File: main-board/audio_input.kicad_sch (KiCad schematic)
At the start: 46 parts, among them J4 NCJ6FA-H-0, J6 NCJ6FA-H-0, Q1 MMBT3904, Q2 MMBT3906, Q3 MMBT3906, Q4 MMBT3904, U4 THAT1246, U5 THAT1246, U6 OPA1656ID, U7 LM2903

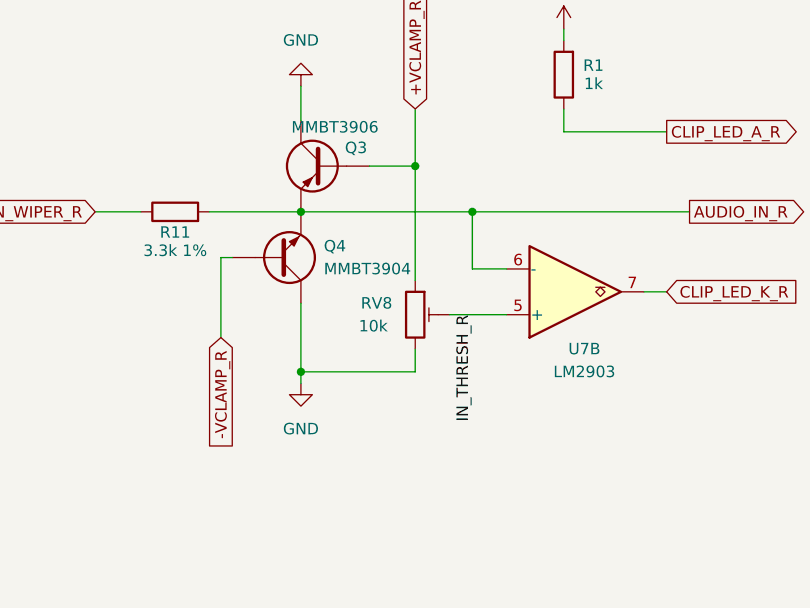
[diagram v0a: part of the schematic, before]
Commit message: swap and label rv8/7 so they lay out clearly
fixes #21
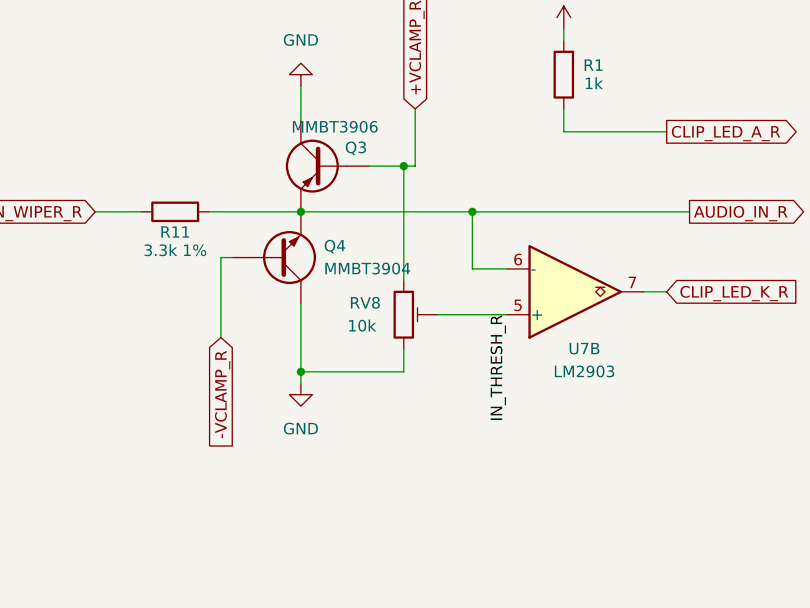
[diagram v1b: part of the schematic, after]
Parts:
- RV7: Label (none) -> ICT_L
- RV8: Label (none) -> ICT_R
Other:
- moved on the sheet: RV8
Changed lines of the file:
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@@
 	)
 	(junction
+		(at 170.18 104.14)
+		(diameter 0)
+		(color 0 0 0 0)
+	)
+	(junction
 		(at 88.9 166.37)
 		(diameter 0)
@@
 	)
 	(junction
-		(at 171.45 104.14)
-		(diameter 0)
-		(color 0 0 0 0)
-	)
-	(junction
 		(at 48.26 149.86)
 		(diameter 0)
@@
 	(wire
 		(pts
-			(xy 166.37 104.14) (xy 171.45 104.14)
+			(xy 166.37 104.14) (xy 170.18 104.14)
 		)
 		(stroke
@@
 	(wire
 		(pts
-			(xy 175.26 120.65) (xy 181.61 120.65)
+			(xy 173.99 120.65) (xy 181.61 120.65)
 		)
 		(stroke
@@
 	(wire
 		(pts
-			(xy 171.45 116.84) (xy 171.45 104.14)
+			(xy 170.18 116.84) (xy 170.18 104.14)
 		)
 		(stroke
@@
 	(wire
 		(pts
-			(xy 171.45 124.46) (xy 171.45 127)
+			(xy 170.18 124.46) (xy 170.18 127)
 		)
 		(stroke
@@
 	(wire
 		(pts
-			(xy 171.45 127) (xy 158.75 127)
+			(xy 170.18 127) (xy 158.75 127)
 		)
 		(stroke
@@
 	(wire
 		(pts
+			(xy 170.18 104.14) (xy 171.45 104.14)
+		)
+		(stroke
+			(width 0)
+			(type default)
+		)
+	)
+	(wire
+		(pts
 			(xy 135.89 166.37) (xy 135.89 172.72)
 		)
@@
 	)
 	(label "IN_THRESH_R"
-		(at 177.8 120.65 270)
+		(at 181.61 120.65 270)
 		(effects
 			(font
@@
 		(lib_name "R_Potentiometer_Trim_1")
 		(lib_id "Device:R_Potentiometer_Trim")
-		(at 171.45 120.65 0)
+		(at 170.18 120.65 0)
 		(unit 1)
 		(exclude_from_sim no)
@@
 		(dnp no)
 		(property "Reference" "RV8"
-			(at 168.91 119.3799 0)
+			(at 167.64 119.3799 0)
 			(effects
 				(font
@@
 		)
 		(property "Value" "10k"
-			(at 168.402 121.92 0)
+			(at 167.132 121.92 0)
 			(effects
 				(font
@@
 		)
 		(property "Footprint" "Potentiometer_THT:Potentiometer_Bourns_3296W_Vertical"
-			(at 171.45 120.65 0)
+			(at 170.18 120.65 0)
 			(effects
 				(font
@@
 		)
 		(property "Datasheet" "~"
-			(at 171.45 120.65 0)
+			(at 170.18 120.65 0)
 			(effects
 				(font
@@
 		)
 		(property "Description" "Multi-Turn Trim-potentiometer"
-			(at 171.45 120.65 0)
+			(at 170.18 120.65 0)
+			(effects
+				(font
+					(size 1.27 1.27)
+				)
+				(hide yes)
+			)
+		)
+		(property "Label" "ICT_R"
+			(at 170.942 124.46 0)
 			(effects
 				(font
@@
 			(at 171.45 58.42 0)
 			(effects
+				(font
+					(size 1.27 1.27)
+				)
+				(hide yes)
+			)
+		)
+		(property "Label" "ICT_L"
+			(at 171.45 58.42 0)
+			(effects

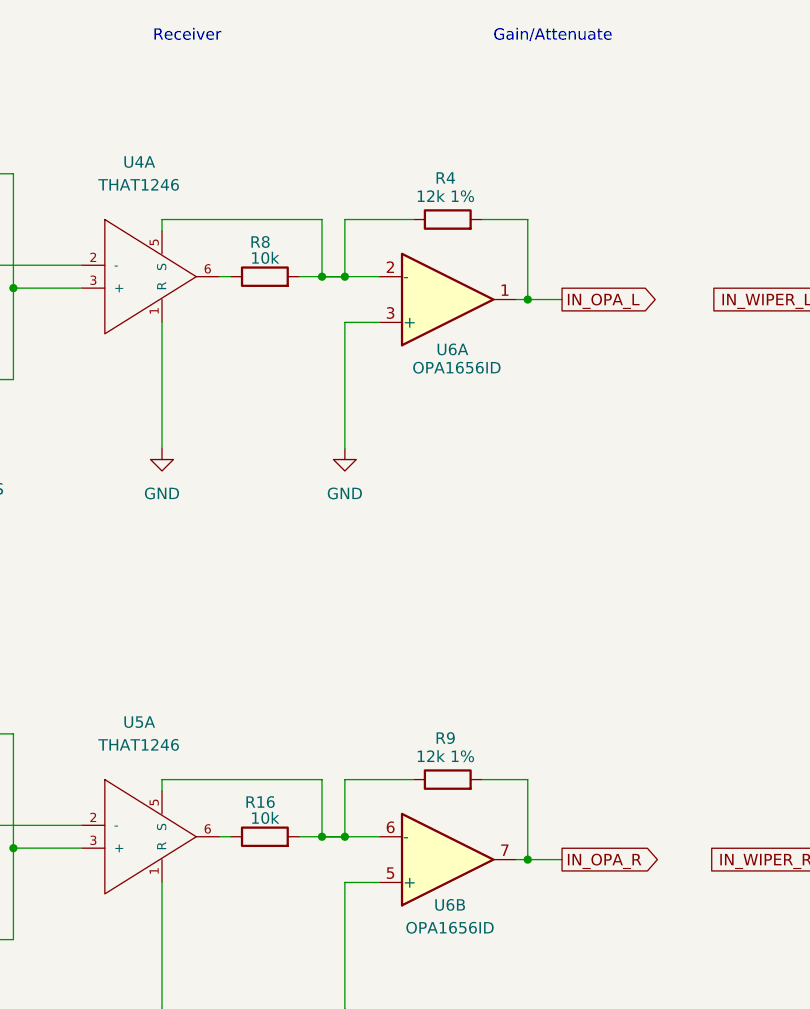
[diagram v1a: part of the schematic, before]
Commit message: fix sense error for output topology
fixes #20
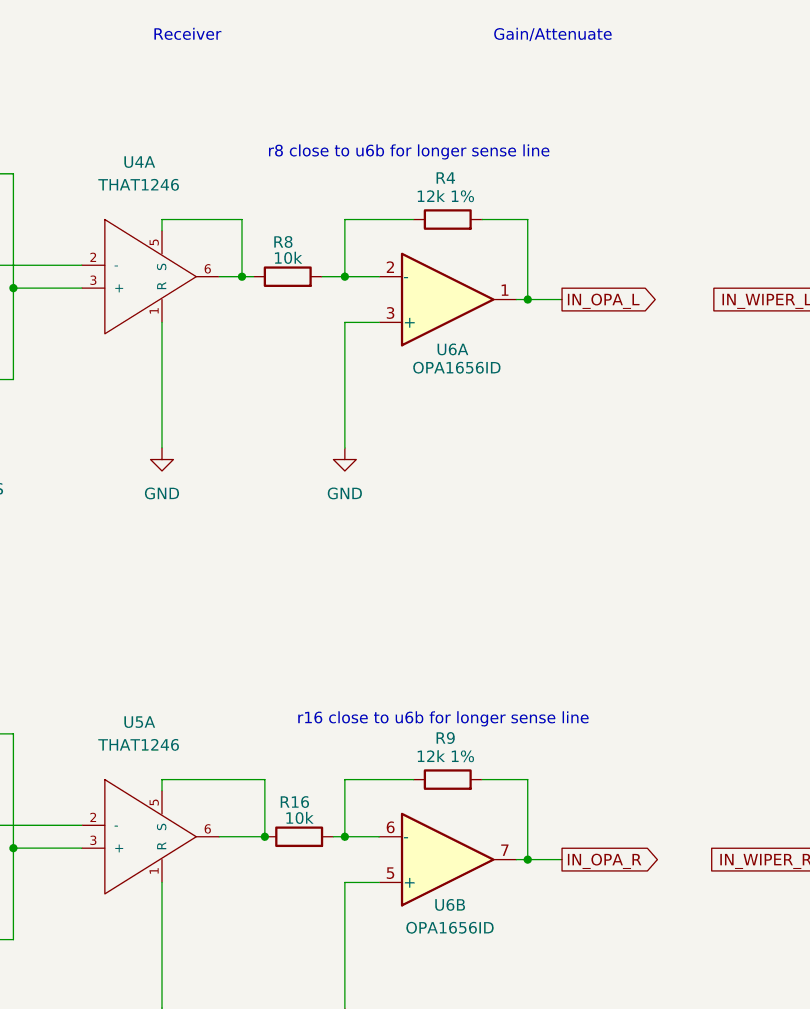
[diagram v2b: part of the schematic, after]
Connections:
- net at R16.2, R9.1, U6.6 (-): no longer U5.5 (S)
- net at R4.1, R8.2, U6.2 (-): no longer U4.5 (S)
- net at R8.1, U4.6: now also U4.5 (S)
- net at R16.1, U5.6: now also U5.5 (S)
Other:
- note added: "r16 close to u6b for longer sense line"
- note added: "r8 close to u6b for longer sense line"
- moved on the sheet: R16, R8
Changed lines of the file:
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@@
 		)
 	)
+	(text "r16 close to u6b for longer sense line\n"
+		(exclude_from_sim no)
+		(at 93.472 93.726 0)
+		(effects
+			(font
+				(size 1.27 1.27)
+			)
+		)
+	)
 	(text "Clipper Reference\n"
 		(exclude_from_sim no)
@@
 		)
 	)
+	(text "r8 close to u6b for longer sense line\n"
+		(exclude_from_sim no)
+		(at 89.662 30.734 0)
+		(effects
+			(font
+				(size 1.27 1.27)
+			)
+		)
+	)
 	(junction
 		(at 170.18 104.14)
@@
 	)
 	(junction
+		(at 73.66 106.68)
+		(diameter 0)
+		(color 0 0 0 0)
+	)
+	(junction
 		(at 88.9 173.99)
 		(diameter 0)
@@
 	)
 	(junction
-		(at 80.01 106.68)
+		(at 45.72 45.72)
 		(diameter 0)
 		(color 0 0 0 0)
 	)
 	(junction
-		(at 45.72 45.72)
+		(at 71.12 44.45)
 		(diameter 0)
 		(color 0 0 0 0)
@@
 	)
 	(junction
-		(at 80.01 44.45)
-		(diameter 0)
-		(color 0 0 0 0)
-	)
-	(junction
 		(at 82.55 44.45)
 		(diameter 0)
@@
 	(wire
 		(pts
-			(xy 68.58 44.45) (xy 69.85 44.45)
+			(xy 68.58 44.45) (xy 71.12 44.45)
 		)
 		(stroke
@@
 		(stroke
 			(width 0)
-			(type dash)
+			(type solid)
 		)
 	)
@@
 	(wire
 		(pts
-			(xy 80.01 100.33) (xy 80.01 106.68)
-		)
-		(stroke
-			(width 0)
-			(type dash)
-		)
-	)
-	(wire
-		(pts
 			(xy 158.75 46.99) (xy 177.8 46.99)
 		)
@@
 	(wire
 		(pts
-			(xy 80.01 106.68) (xy 82.55 106.68)
+			(xy 135.89 163.83) (xy 135.89 166.37)
 		)
 		(stroke
@@
 	(wire
 		(pts
-			(xy 135.89 163.83) (xy 135.89 166.37)
+			(xy 62.23 100.33) (xy 62.23 101.6)
 		)
 		(stroke
 			(width 0)
-			(type default)
+			(type dash)
 		)
 	)
@@
 	(wire
 		(pts
-			(xy 80.01 38.1) (xy 80.01 44.45)
-		)
-		(stroke
-			(width 0)
-			(type dash)
-		)
-	)
-	(wire
-		(pts
-			(xy 62.23 38.1) (xy 80.01 38.1)
-		)
-		(stroke
-			(width 0)
-			(type dash)
-		)
-	)
-	(wire
-		(pts
 			(xy 82.55 111.76) (xy 82.55 125.73)
 		)
@@
 	(wire
 		(pts
-			(xy 77.47 106.68) (xy 80.01 106.68)
-		)
-		(stroke
-			(width 0)
-			(type default)
-		)
-	)
-	(wire
-		(pts
-			(xy 80.01 106.68) (xy 82.55 106.68)
-		)
-		(stroke
-			(width 0)
-			(type dash)
-		)
-	)
-	(wire
-		(pts
 			(xy 238.76 38.1) (xy 238.76 39.37)
 		)
@@
 	(wire
 		(pts
-			(xy 80.01 44.45) (xy 82.55 44.45)
-		)
-		(stroke
-			(width 0)
-			(type default)
-		)
-	)
-	(wire
-		(pts
 			(xy 149.86 52.07) (xy 151.13 52.07)
 		)
@@
 	(wire
 		(pts
-			(xy 68.58 106.68) (xy 69.85 106.68)
+			(xy 68.58 106.68) (xy 73.66 106.68)
 		)
 		(stroke
@@
 	(wire
 		(pts
+			(xy 71.12 38.1) (xy 71.12 44.45)
+		)
+		(stroke
+			(width 0)
+			(type dash)
+		)
+	)
+	(wire
+		(pts
 			(xy 229.87 146.05) (xy 229.87 151.13)
 		)
@@
 	(wire
 		(pts
-			(xy 40.64 63.5) (xy 40.64 50.8)
+			(xy 62.23 100.33) (xy 73.66 100.33)
 		)
 		(stroke
 			(width 0)
-			(type default)
+			(type dash)
 		)
 	)
 	(wire
 		(pts
-			(xy 62.23 100.33) (xy 80.01 100.33)
+			(xy 40.64 63.5) (xy 40.64 50.8)
 		)
 		(stroke
 			(width 0)
-			(type dash)
+			(type default)
 		)
 	)
@@
 	(wire
 		(pts
-			(xy 77.47 44.45) (xy 80.01 44.45)
-		)
-		(stroke
-			(width 0)
-			(type default)
-		)
-	)
-	(wire
-		(pts
 			(xy 238.76 30.48) (xy 238.76 29.21)
 		)
@@
 		(stroke
 			(width 0)
-			(type dash)
+			(type solid)
 		)
 	)
@@
 	(wire
 		(pts
+			(xy 73.66 100.33) (xy 73.66 106.68)
+		)
+		(stroke
+			(width 0)
+			(type dash)
+		)
+	)
+	(wire
+		(pts
 			(xy 48.26 158.75) (xy 52.07 158.75)
 		)
@@
 	(wire
 		(pts
-			(xy 62.23 100.33) (xy 62.23 101.6)
+			(xy 196.85 55.88) (xy 199.39 55.88)
 		)
 		(stroke
 			(width 0)
-			(type dash)
+			(type default)
 		)
 	)
 	(wire
 		(pts
-			(xy 196.85 55.88) (xy 199.39 55.88)
+			(xy 187.96 90.17) (xy 187.96 88.9)
 		)
 		(stroke
@@
 	(wire
 		(pts
-			(xy 187.96 90.17) (xy 187.96 88.9)
+			(xy 187.96 100.33) (xy 199.39 100.33)
 		)
 		(stroke
@@
 	(wire
 		(pts
-			(xy 187.96 100.33) (xy 199.39 100.33)
+			(xy 43.18 40.64) (xy 43.18 43.18)
 		)
 		(stroke
@@
 	(wire
 		(pts
-			(xy 43.18 40.64) (xy 43.18 43.18)
+			(xy 148.59 46.99) (xy 158.75 46.99)
 		)
 		(stroke
@@
 	(wire
 		(pts
-			(xy 148.59 46.99) (xy 158.75 46.99)
+			(xy 148.59 109.22) (xy 158.75 109.22)
 		)
 		(stroke
@@
 	(wire
 		(pts
-			(xy 148.59 109.22) (xy 158.75 109.22)
+			(xy 81.28 106.68) (xy 82.55 106.68)
 		)
 		(stroke
@@
 		(stroke
 			(width 0)
-			(type dash)
+			(type solid)
 		)
 	)
@@
 	(wire
 		(pts
+			(xy 62.23 38.1) (xy 71.12 38.1)
+		)
+		(stroke
+			(width 0)
+			(type dash)
+		)
+	)
+	(wire
+		(pts
 			(xy 31.75 189.23) (xy 31.75 187.96)
 		)
@@
 	(wire
 		(pts
+			(xy 71.12 44.45) (xy 72.39 44.45)
+		)
+		(stroke
+			(width 0)
+			(type default)
+		)
+	)
+	(wire
+		(pts
 			(xy 237.49 160.02) (xy 237.49 161.29)
 		)
@@
 	(symbol
 		(lib_id "Device:R")
-		(at 73.66 44.45 90)
+		(at 76.2 44.45 90)
 		(unit 1)
 		(exclude_from_sim no)
@@
 		(dnp no)
 		(property "Reference" "R8"
-			(at 73.152 40.64 90)
+			(at 75.692 40.64 90)
 			(effects
 				(font
@@
 		)
 		(property "Value" "10k"
-			(at 73.66 42.418 90)
+			(at 76.2 42.418 90)
 			(effects
 				(font
@@
 		)
 		(property "Footprint" "Resistor_SMD:R_0805_2012Metric"
-			(at 73.66 46.228 90)
+			(at 76.2 46.228 90)
 			(effects
 				(font
@@
 		)
 		(property "Datasheet" "~"
-			(at 73.66 44.45 0)
+			(at 76.2 44.45 0)
 			(effects
 				(font
@@
 		)
 		(property "Description" "Resistor"
-			(at 73.66 44.45 0)
+			(at 76.2 44.45 0)
 			(effects
 				(font
@@
 		)
 		(property "Placement" "In signal path between THAT1246 output and protection diodes."
-			(at 73.66 44.45 0)
+			(at 76.2 44.45 0)
 			(effects
 				(font
@@
 	(symbol
 		(lib_id "Device:R")
-		(at 73.66 106.68 90)
+		(at 77.47 106.68 90)
 		(unit 1)
 		(exclude_from_sim no)
@@
 		(dnp no)
 		(property "Reference" "R16"
-			(at 73.152 102.87 90)
+			(at 76.962 102.87 90)
 			(effects
 				(font
@@
 		)
 		(property "Value" "10k"
-			(at 73.66 104.648 90)
+			(at 77.47 104.648 90)
 			(effects
 				(font
@@
 		)
 		(property "Footprint" "Resistor_SMD:R_0805_2012Metric"
-			(at 73.66 108.458 90)
+			(at 77.47 108.458 90)
 			(effects
 				(font
@@
 		)
 		(property "Datasheet" "~"
-			(at 73.66 106.68 0)
+			(at 77.47 106.68 0)
 			(effects
 				(font
@@
 		)
 		(property "Description" "Resistor"
-			(at 73.66 106.68 0)
+			(at 77.47 106.68 0)
 			(effects
 				(font
@@
 		)
 		(property "Placement" "In signal path between THAT1246 output and protection diodes."
-			(at 73.66 106.68 0)
+			(at 77.47 106.68 0)
 			(effects
 				(font

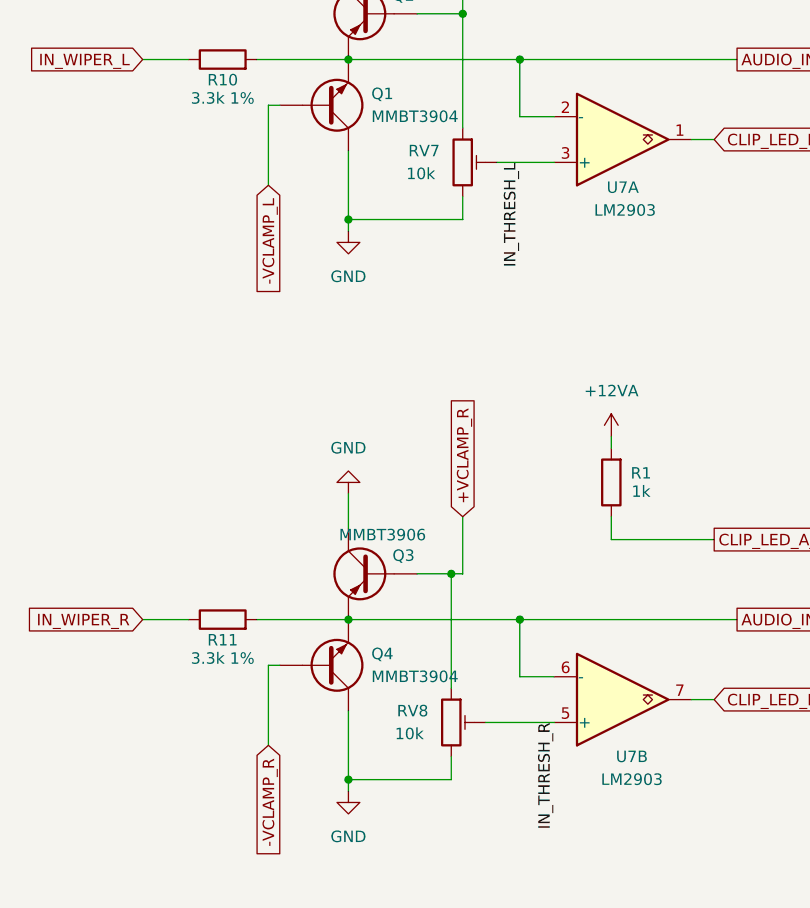
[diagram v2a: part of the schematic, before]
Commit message: make threshold trimmer 100k so it doesn't drag down the clamp ref +ve rail
fixes #19
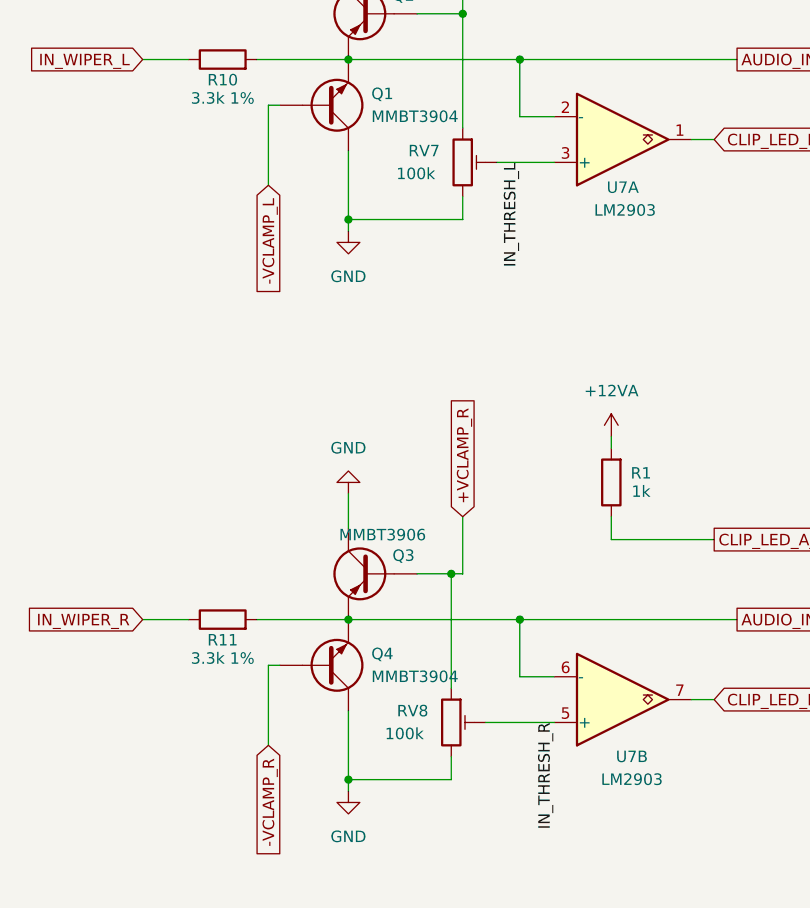
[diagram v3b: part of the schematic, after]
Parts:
- RV7, RV8: value 10k -> 100k
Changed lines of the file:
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@@
 			)
 		)
-		(property "Value" "10k"
+		(property "Value" "100k"
 			(at 167.132 121.92 0)
 			(effects
@@
 			)
 		)
-		(property "Value" "10k"
+		(property "Value" "100k"
 			(at 168.402 59.69 0)
 			(effects

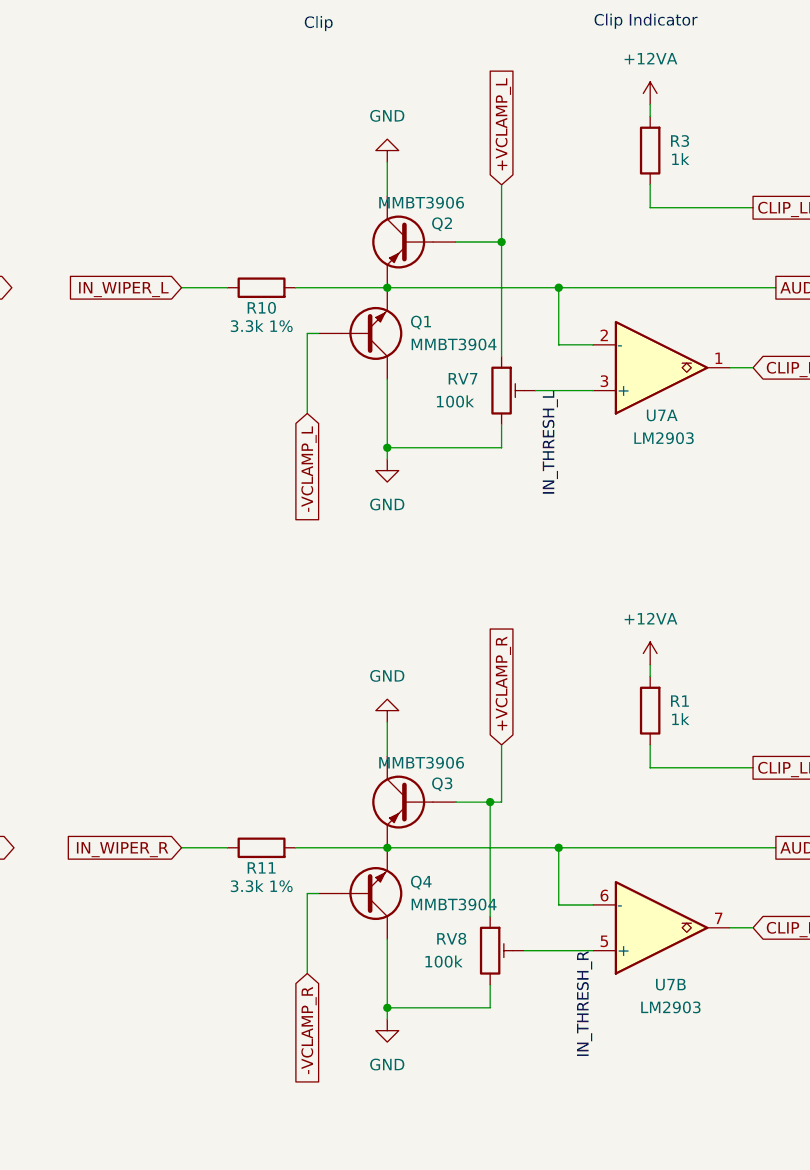
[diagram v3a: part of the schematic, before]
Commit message: fix footprint on the clamp transistors
fixes #18
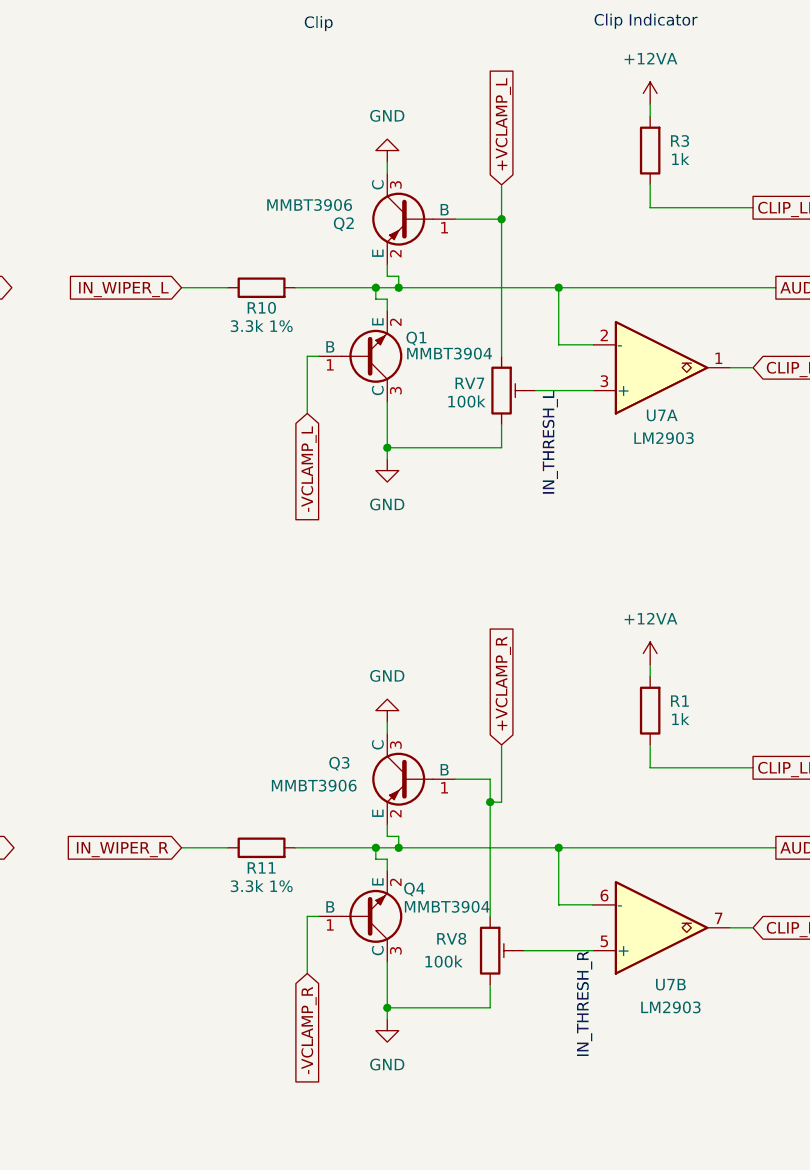
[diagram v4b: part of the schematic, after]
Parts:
- Q1, Q4: symbol Transistor_BJT:2N3904 -> Transistor_BJT:MMBT3904
- Q2, Q3: symbol Transistor_BJT:2N3906 -> Transistor_BJT:MMBT3906
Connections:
- net +VCLAMP_L: now also Q2.1 (B); no longer Q2.2 (B)
- net +VCLAMP_R: now also Q3.1 (B); no longer Q3.2 (B)
- net -VCLAMP_L: now also Q1.1 (B); no longer Q1.2 (B)
- net -VCLAMP_R: now also Q4.1 (B); no longer Q4.2 (B)
- net AUDIO_IN_L: now also Q1.2 (E), Q2.2 (E); no longer Q1.1 (E), Q2.1 (E)
- net AUDIO_IN_R: now also Q3.2 (E), Q4.2 (E); no longer Q3.1 (E), Q4.1 (E)
